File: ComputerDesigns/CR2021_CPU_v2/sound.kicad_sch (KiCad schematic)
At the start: 5 parts, among them U1 LM324

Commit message: add sound
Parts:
- removed C1: 4.7nF, symbol Device:C
- removed C2: 2.2nF, symbol Device:C
- removed R1, R2: 10k, symbol Device:R
- removed unit 1 of U1
- added $4002, $4003: 74LS273, Package_DIP:DIP-20_W7.62mm, symbol 74xx:74LS273
- added C4, C5: 22pF, symbol Device:C
- added C6: 4.7n, symbol Device:C
- added J3: Conn_STK500v2, Connector_IDC:IDC-Header_2x03_P2.54mm_Vertical, symbol Custom:Conn_STK500v2
- added LS1: Speaker, Connector_PinHeader_2.54mm:PinHeader_1x02_P2.54mm_Vertical, symbol Device:Speaker
- added R4, R5, R6: 10k, symbol Device:R
- added unit 2 of U1
- added U6: ATmega328-P, Package_DIP:DIP-28_W7.62mm, symbol MCU_Microchip_ATmega:ATmega328-P
- added Y2: 16MHz, symbol Device:Crystal
- U1: footprint (none) -> Package_DIP:DIP-14_W7.62mm
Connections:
- net +5V: now also $4002.1 (~{Mr}), $4002.20 (VCC), $4003.1 (~{Mr}), $4003.20 (VCC), J3.2 (VCC), U6.20 (AVCC), U6.7 (VCC)
- net GND: now also $4002.10 (GND), $4003.10 (GND), C4.2, C5.2, C6.2, J3.6 (GND), LS1.2, R6.2, U6.22 (GND), U6.8 (GND)
- new net: R4.1, U6.12 (PD6)
- new net: C6.1, R4.2, R5.1
- new net: C5.1, U6.9 (XTAL1/PB6), Y2.2
- new net: $4003.2 (Q0), U6.4 (PD2)
- new net: $4003.5 (Q1), U6.5 (PD3)
- new net: LS1.1, U1.6 (-), U1.7
- new net: C4.1, U6.10 (XTAL2/PB7), Y2.1
- new net: R5.2, R6.1, U1.5 (+)
- new net: $4002.12 (Q4), U6.27 (PC4)
- new net: $4002.15 (Q5), U6.28 (PC5)
- new net: $4002.16 (Q6), U6.2 (PD0)
- new net: $4002.19 (Q7), U6.3 (PD1)
- new net: $4002.2 (Q0), U6.23 (PC0)
- new net: $4002.5 (Q1), U6.24 (PC1)
- new net: $4002.6 (Q2), U6.25 (PC2)
- new net: $4002.9 (Q3), U6.26 (PC3)
- new net: J3.5 (RST), U6.1 (~{RESET}/PC6)
- new net: J3.4 (MOSI), U6.17 (PB3)
- new net: J3.1 (MISO), U6.18 (PB4)
- new net: J3.3 (SCK), U6.19 (PB5)
- new net $4002_OUT: $4002.11 (Cp)
- new net $4003_OUT: $4003.11 (Cp)
- new net DATA0: $4002.3 (D0), $4003.3 (D0)
- new net DATA1: $4002.4 (D1), $4003.4 (D1)
- new net DATA2: $4002.7 (D2), $4003.7 (D2)
- new net DATA3: $4002.8 (D3), $4003.8 (D3)
- new net DATA4: $4002.13 (D4), $4003.13 (D4)
- new net DATA5: $4002.14 (D5), $4003.14 (D5)
- new net DATA6: $4002.17 (D6), $4003.17 (D6)
- new net DATA7: $4002.18 (D7), $4003.18 (D7)
- new net R/!W: U6.6 (PD4)
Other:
- note added: "This part needs extra work before we make the PCB. Perhaps an active filter, or at least make the right calculations! It also needs a volumne knob"

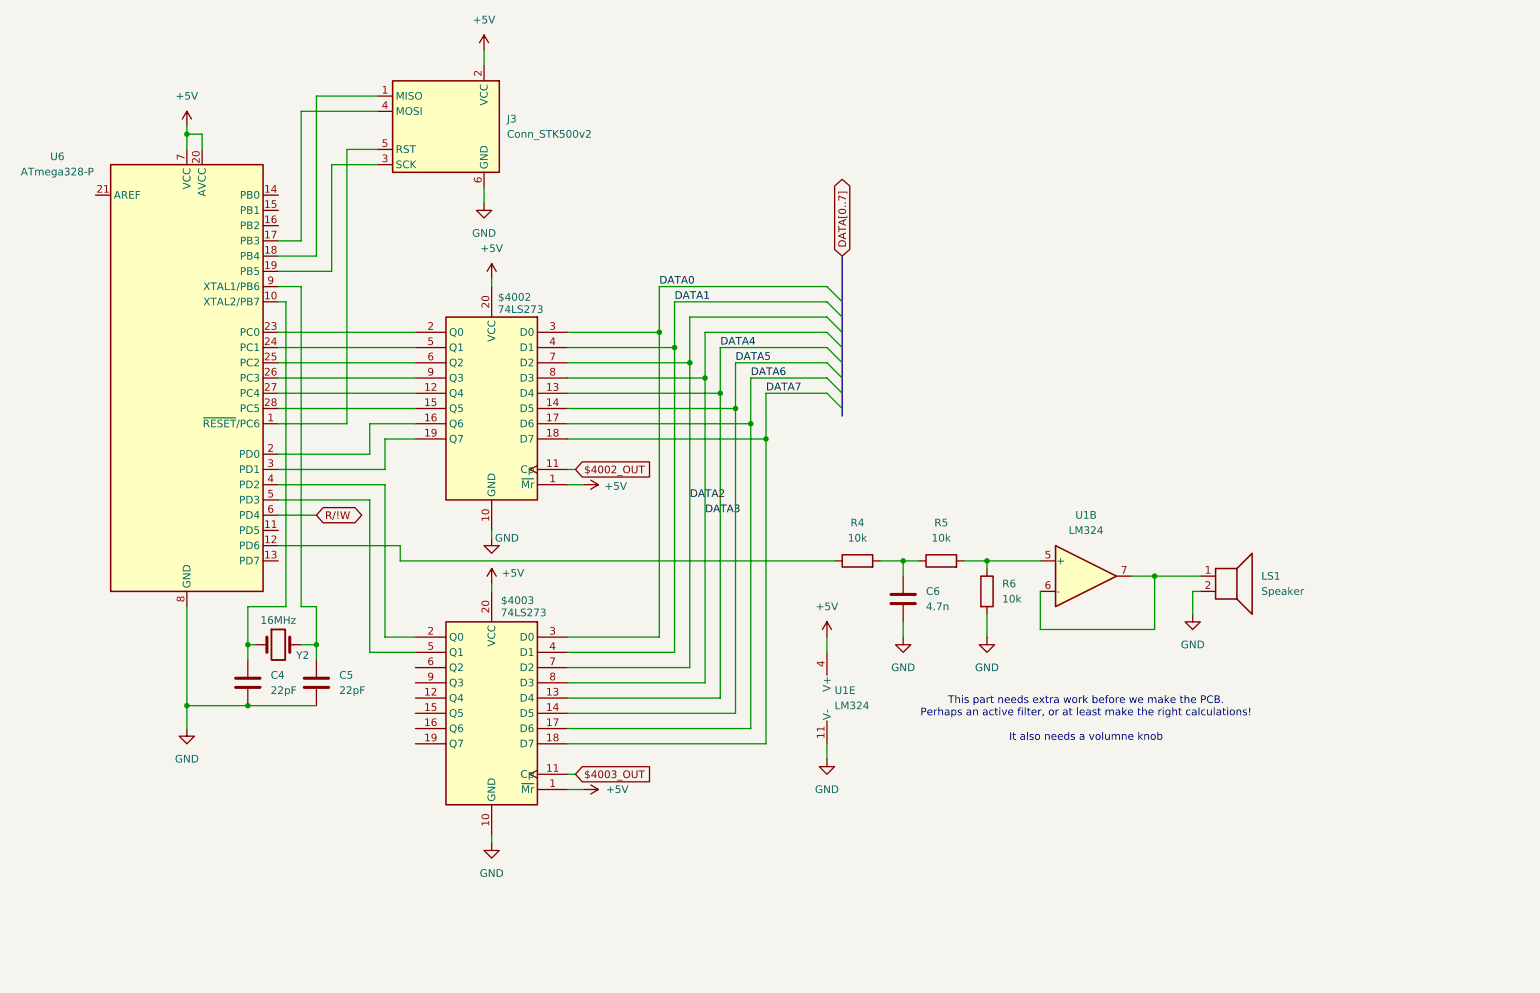
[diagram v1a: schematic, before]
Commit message: updated schematic with opamp mixer
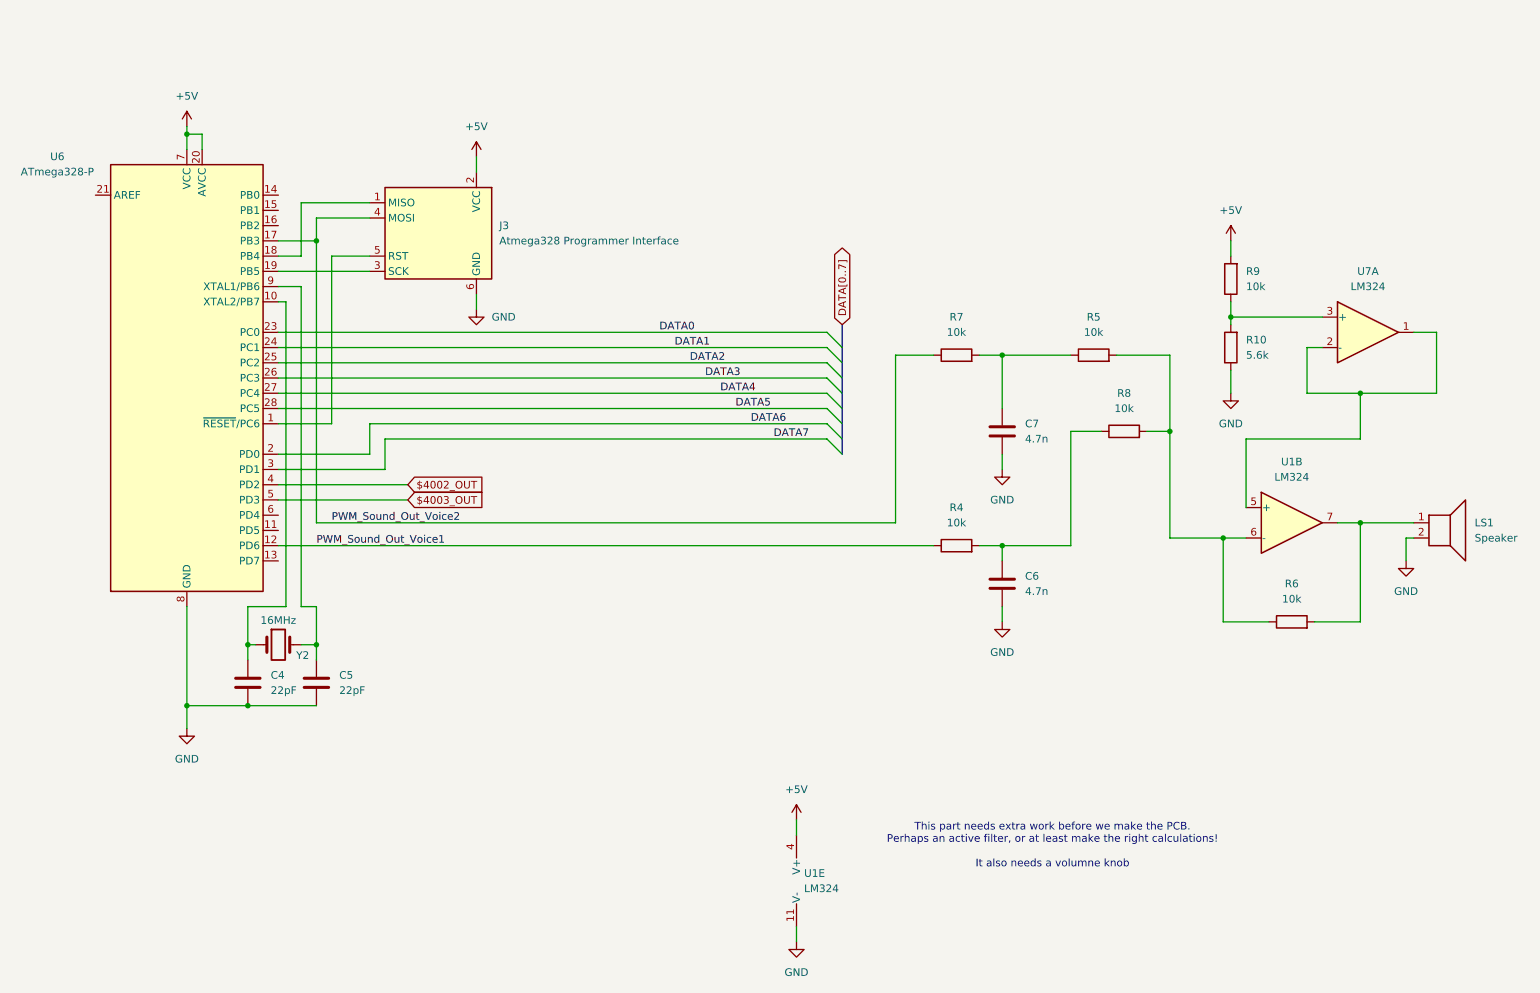
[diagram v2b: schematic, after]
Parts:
- removed $4002, $4003: 74LS273, Package_DIP:DIP-20_W7.62mm, symbol 74xx:74LS273
- added C7: 4.7n, symbol Device:C
- added R10: 5.6k, symbol Device:R
- added R7, R8, R9: 10k, symbol Device:R
- added U7: LM324, Package_DIP:DIP-14_W7.62mm, symbol Amplifier_Operational:LM324
- J3: value Conn_STK500v2 -> Atmega328 Programmer Interface
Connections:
- net $4002_OUT: now also U6.4 (PD2)
- net $4003_OUT: now also U6.5 (PD3)
- net +5V: now also R9.2
- net DATA0: now also U6.23 (PC0)
- net DATA1: now also U6.24 (PC1)
- net DATA2: now also U6.25 (PC2)
- net DATA3: now also U6.26 (PC3)
- net DATA4: now also U6.27 (PC4)
- net DATA5: now also U6.28 (PC5)
- net DATA6: now also U6.2 (PD0)
- net DATA7: now also U6.3 (PD1)
- net GND: now also C7.2, R10.1; no longer R6.2
- net PWM_Sound_Out_Voice1: now reaches R4.1, U6.12 (PD6)
- net at C6.1, R4.2: now also R8.1; no longer R5.1
- net at LS1.1, U1.7: now also R6.2; no longer U1.6 (-)
- net at R5.2, R6.1: now also U1.6 (-), R8.2; no longer U1.5 (+)
- net PWM_Sound_Out_Voice2: now reaches J3.4 (MOSI), U6.17 (PB3)
- net PWM_Sound_Out_Voice2: now also R7.1
- net R/!W: no longer names the net of U6.6 (PD4)
- new net: R10.2, R9.1, U7.3 (+)
- new net: U1.5 (+), U7.1, U7.2 (-)
- new net: C7.1, R5.1, R7.2
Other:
- moved on the sheet: C6, J3, LS1, R4, R5, R6, U1B, U1E

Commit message: update schematics
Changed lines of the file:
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@@
 	(bus
 		(pts
-			(xy 168.91 72.39) (xy 168.91 76.2)
+			(xy 168.91 69.85) (xy 168.91 76.2)
 		)
 		(stroke
@@
 	(global_label "DATA[0..7]"
 		(shape bidirectional)
-		(at 168.91 72.39 90)
+		(at 168.91 69.85 90)
 		(fields_autoplaced yes)
 		(effects
@@
 		)
 		(property "Intersheetrefs" "${INTERSHEET_REFS}"
-			(at 168.91 59.3697 90)
+			(at 168.91 56.8297 90)
 			(effects
 				(font
@@
 		)
 		(instances
-			(project ""
+			(project "CR2021_CPU_v2"
 				(path "/5ba384c5-5050-42b4-8e60-2da7b065216b/c84ba92a-28ca-438c-b0db-03d23848e5c0"
 					(reference "R4")
@@
 		)
 		(instances
-			(project ""
+			(project "CR2021_CPU_v2"
 				(path "/5ba384c5-5050-42b4-8e60-2da7b065216b/c84ba92a-28ca-438c-b0db-03d23848e5c0"
 					(reference "U1")
@@
 		)
 		(instances
-			(project ""
+			(project "CR2021_CPU_v2"
 				(path "/5ba384c5-5050-42b4-8e60-2da7b065216b/c84ba92a-28ca-438c-b0db-03d23848e5c0"
 					(reference "C6")
@@
 		)
 		(instances
-			(project ""
+			(project "CR2021_CPU_v2"
 				(path "/5ba384c5-5050-42b4-8e60-2da7b065216b/c84ba92a-28ca-438c-b0db-03d23848e5c0"
 					(reference "LS1")
@@
 		)
 		(instances
-			(project ""
+			(project "CR2021_CPU_v2"
 				(path "/5ba384c5-5050-42b4-8e60-2da7b065216b/c84ba92a-28ca-438c-b0db-03d23848e5c0"
 					(reference "#PWR03")
@@
 		)
 		(instances
-			(project ""
+			(project "CR2021_CPU_v2"
 				(path "/5ba384c5-5050-42b4-8e60-2da7b065216b/c84ba92a-28ca-438c-b0db-03d23848e5c0"
 					(reference "#PWR05")
@@
 		)
 		(instances
-			(project ""
+			(project "CR2021_CPU_v2"
 				(path "/5ba384c5-5050-42b4-8e60-2da7b065216b/c84ba92a-28ca-438c-b0db-03d23848e5c0"
 					(reference "#PWR015")
@@
 		)
 		(instances
-			(project ""
+			(project "CR2021_CPU_v2"
 				(path "/5ba384c5-5050-42b4-8e60-2da7b065216b/c84ba92a-28ca-438c-b0db-03d23848e5c0"
 					(reference "C4")
@@
 		)
 		(instances
-			(project ""
+			(project "CR2021_CPU_v2"
 				(path "/5ba384c5-5050-42b4-8e60-2da7b065216b/c84ba92a-28ca-438c-b0db-03d23848e5c0"
 					(reference "#PWR04")
@@
 		)
 		(instances
-			(project ""
+			(project "CR2021_CPU_v2"
 				(path "/5ba384c5-5050-42b4-8e60-2da7b065216b/c84ba92a-28ca-438c-b0db-03d23848e5c0"
 					(reference "R5")
@@
 		)
 		(instances
-			(project ""
+			(project "CR2021_CPU_v2"
 				(path "/5ba384c5-5050-42b4-8e60-2da7b065216b/c84ba92a-28ca-438c-b0db-03d23848e5c0"
 					(reference "U1")
@@
 		)
 		(instances
-			(project ""
+			(project "CR2021_CPU_v2"
 				(path "/5ba384c5-5050-42b4-8e60-2da7b065216b/c84ba92a-28ca-438c-b0db-03d23848e5c0"
 					(reference "Y2")
@@
 		)
 		(instances
-			(project ""
+			(project "CR2021_CPU_v2"
 				(path "/5ba384c5-5050-42b4-8e60-2da7b065216b/c84ba92a-28ca-438c-b0db-03d23848e5c0"
 					(reference "#PWR012")
@@
 		)
 		(instances
-			(project ""
+			(project "CR2021_CPU_v2"
 				(path "/5ba384c5-5050-42b4-8e60-2da7b065216b/c84ba92a-28ca-438c-b0db-03d23848e5c0"
 					(reference "U6")
@@
 		)
 		(instances
-			(project ""
+			(project "CR2021_CPU_v2"
 				(path "/5ba384c5-5050-42b4-8e60-2da7b065216b/c84ba92a-28ca-438c-b0db-03d23848e5c0"
 					(reference "#PWR013")
@@
 		)
 		(instances
-			(project ""
+			(project "CR2021_CPU_v2"
 				(path "/5ba384c5-5050-42b4-8e60-2da7b065216b/c84ba92a-28ca-438c-b0db-03d23848e5c0"
 					(reference "J3")
@@
 		)
 		(instances
-			(project ""
+			(project "CR2021_CPU_v2"
 				(path "/5ba384c5-5050-42b4-8e60-2da7b065216b/c84ba92a-28ca-438c-b0db-03d23848e5c0"
 					(reference "R6")
